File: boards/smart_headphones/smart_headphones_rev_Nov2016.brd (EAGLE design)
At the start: 51.7 x 39.4 mm, 14 parts, among them U1 ATMEGA328P_PDIP

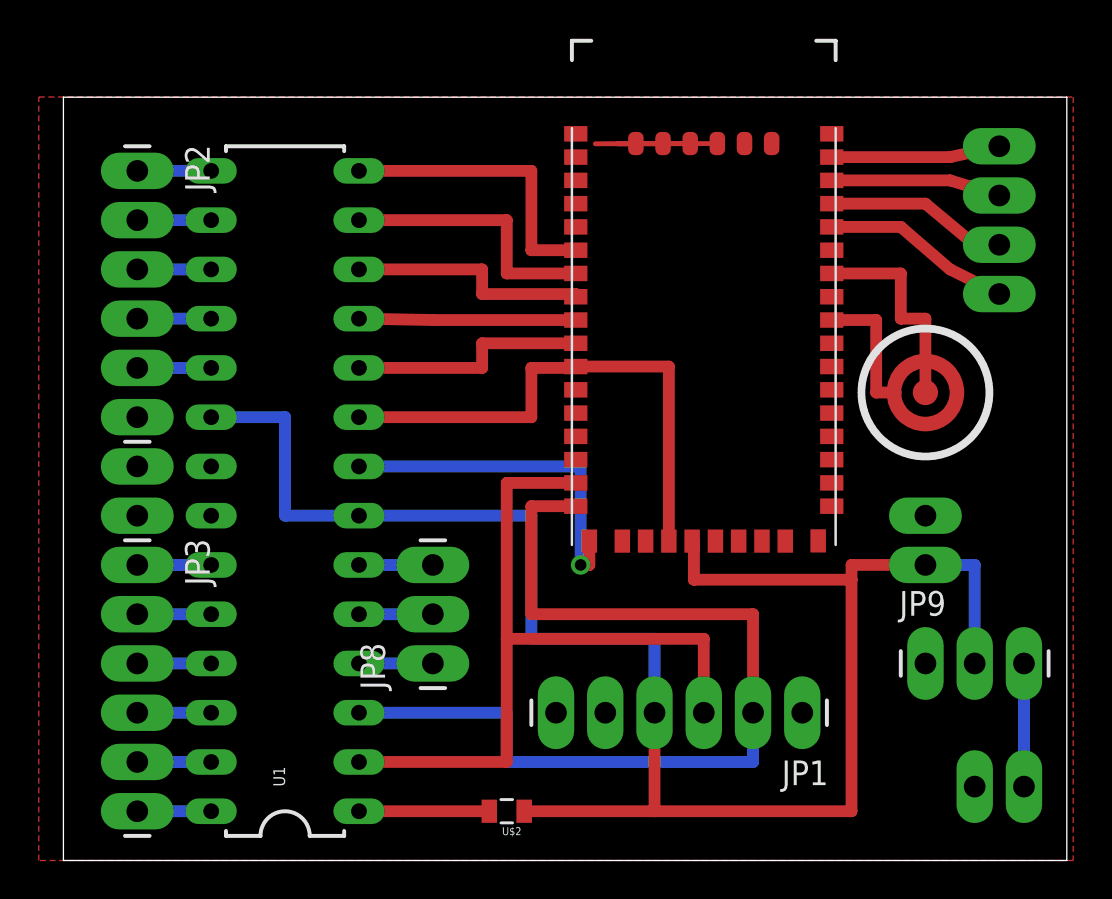
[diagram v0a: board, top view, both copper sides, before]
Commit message: Fixed bug (two control signals connected)
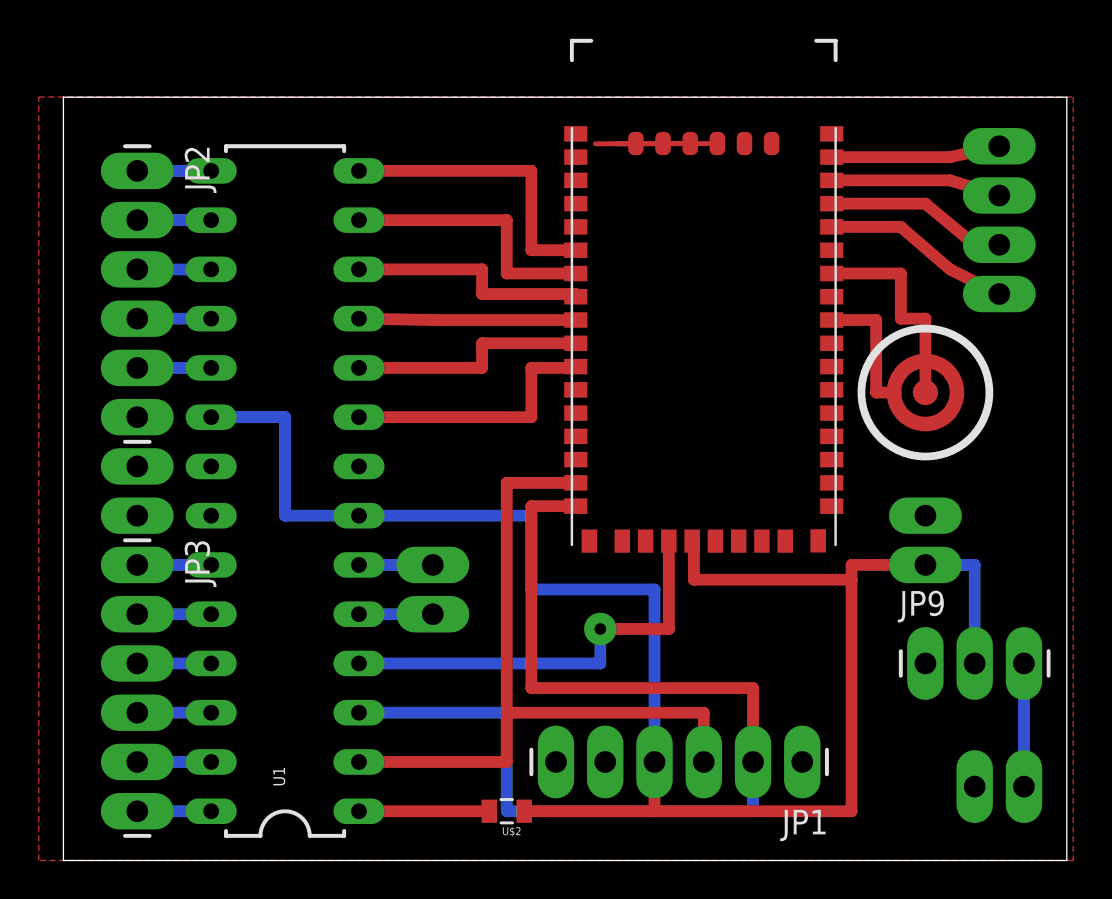
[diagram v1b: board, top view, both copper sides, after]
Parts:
- JP8: value (none) -> M02PTH3; device Finn-lbr-rev1:1X03_LONGPADS -> Finn-lbr-rev1:1X02_LONGPADS
- moved JP1 2.54 mm to (38.1, 24.1)
- moved JP8 2.54 mm to (19.1, 31.8)
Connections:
- removed net N$17: JP8.1, U1.4
- new net PWREN: U$1.19, U1.4
- net N$18: now also JP8.1; no longer JP8.2
- net N$19: now also JP8.2; no longer JP8.3
- net PB6: no longer U$1.19
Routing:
- net PWREN: track 0.00 -> 22.3 mm, vias 0 -> 1
- net GND: track 28.2 -> 10.0 mm, vias 1 -> 0
- net PB6: track 27.6 -> 13.8 mm
- net N$10: track 49.8 -> 54.9 mm
- net N$17: track 3.81 -> 0.00 mm
- net N$5: track 39.5 -> 38.3 mm
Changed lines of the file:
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@@
 <?xml version="1.0" encoding="utf-8"?>
 <!DOCTYPE eagle SYSTEM "eagle.dtd">
-<eagle version="7.1.0">
+<eagle version="7.7.0">
 <drawing>
 <settings>
@@
 </autorouter>
 <elements>
-<element name="JP1" library="Finn-lbr-rev1" package="1X06_LONGPADS" value="" x="38.1" y="26.67" rot="R180"/>
+<element name="JP1" library="Finn-lbr-rev1" package="1X06_LONGPADS" value="" x="38.1" y="24.13" rot="R180"/>
 <element name="JP3" library="Finn-lbr-rev1" package="1X06_LONGPADS" value="" x="3.81" y="34.29" rot="R270"/>
 <element name="U$1" library="Finn-lbr-rev1" package="RN-52" value="BLUETOOTH-RN-52" x="33.02" y="46.99"/>
@@
 <element name="JP6" library="Finn-lbr-rev1" package="1X02_LONGPADS" value="M02PTH3" x="44.45" y="36.83" rot="R270"/>
 <element name="JP7" library="Finn-lbr-rev1" package="1X02_LONGPADS" value="M02PTH3" x="3.81" y="39.37" rot="R270"/>
-<element name="JP8" library="Finn-lbr-rev1" package="1X03_LONGPADS" value="" x="19.05" y="29.21" rot="R90"/>
 <element name="JP9" library="Finn-lbr-rev1" package="1X03_LONGPADS" value="" x="44.45" y="29.21"/>
 <element name="JP10" library="Finn-lbr-rev1" package="1X02_LONGPADS" value="M02PTH3" x="49.53" y="22.86" rot="R180"/>
+<element name="JP8" library="Finn-lbr-rev1" package="1X02_LONGPADS" value="M02PTH3" x="19.05" y="31.75" rot="R90"/>
 </elements>
 <signals>
@@
 <contactref element="JP1" pad="4"/>
 <wire x1="23.76" y1="21.59" x2="30.48" y2="21.59" width="0.6096" layer="1"/>
-<wire x1="30.48" y1="21.59" x2="30.48" y2="26.67" width="0.6096" layer="1"/>
+<wire x1="30.48" y1="21.59" x2="30.48" y2="24.13" width="0.6096" layer="1"/>
 <wire x1="32.42" y1="35.52" x2="32.512" y2="35.52" width="0.6096" layer="1"/>
 <wire x1="32.512" y1="35.52" x2="32.512" y2="33.528" width="0.6096" layer="1"/>
@@
 <wire x1="40.64" y1="21.59" x2="30.48" y2="21.59" width="0.6096" layer="1"/>
 <wire x1="15.24" y1="36.83" x2="24.13" y2="36.83" width="0.6096" layer="16"/>
-<wire x1="24.13" y1="36.83" x2="24.13" y2="30.48" width="0.6096" layer="16"/>
-<wire x1="24.13" y1="30.48" x2="30.48" y2="30.48" width="0.6096" layer="16"/>
-<wire x1="30.48" y1="30.48" x2="30.48" y2="26.67" width="0.6096" layer="16"/>
+<wire x1="24.13" y1="36.83" x2="24.13" y2="33.02" width="0.6096" layer="16"/>
+<wire x1="24.13" y1="33.02" x2="30.48" y2="33.02" width="0.6096" layer="16"/>
+<wire x1="30.48" y1="33.02" x2="30.48" y2="24.13" width="0.6096" layer="16"/>
 <contactref element="U1" pad="20"/>
 <wire x1="7.62" y1="41.91" x2="11.43" y2="41.91" width="0.6096" layer="16"/>
@@
 </signal>
 <signal name="PB6">
-<contactref element="U$1" pad="19"/>
 <contactref element="U1" pad="9"/>
 <contactref element="U$1" pad="10"/>
@@
 <wire x1="24.13" y1="44.45" x2="26.42" y2="44.45" width="0.6096" layer="1"/>
 <wire x1="26.42" y1="44.45" x2="26.42" y2="44.52" width="0.6096" layer="1"/>
-<wire x1="26.42" y1="44.52" x2="31.22" y2="44.52" width="0.6096" layer="1"/>
-<wire x1="31.22" y1="44.52" x2="31.22" y2="35.52" width="0.6096" layer="1"/>
 </signal>
 <signal name="PB0">
@@
 <wire x1="28.575" y1="56.007" x2="33.72" y2="56.02" width="0.254" layer="1"/>
 <contactref element="JP2" pad="6"/>
-<wire x1="15.24" y1="39.37" x2="26.67" y2="39.37" width="0.6096" layer="16"/>
-<wire x1="26.67" y1="39.37" x2="26.67" y2="34.29" width="0.6096" layer="16"/>
-<via x="26.67" y="34.29" extent="1-16" drill="0.6" shape="square"/>
-<wire x1="26.67" y1="34.29" x2="27.12" y2="34.29" width="0.6096" layer="1"/>
-<wire x1="27.12" y1="34.29" x2="27.12" y2="35.52" width="0.6096" layer="1"/>
 <contactref element="JP7" pad="1"/>
 <contactref element="JP7" pad="2"/>
@@
 <contactref element="JP1" pad="3"/>
 <wire x1="26.42" y1="38.52" x2="22.86" y2="38.52" width="0.6096" layer="1"/>
-<wire x1="22.86" y1="38.52" x2="22.86" y2="30.48" width="0.6096" layer="1"/>
-<wire x1="22.86" y1="30.48" x2="33.02" y2="30.48" width="0.6096" layer="1"/>
-<wire x1="33.02" y1="30.48" x2="33.02" y2="26.67" width="0.6096" layer="1"/>
+<wire x1="22.86" y1="38.52" x2="22.86" y2="26.67" width="0.6096" layer="1"/>
+<wire x1="22.86" y1="26.67" x2="33.02" y2="26.67" width="0.6096" layer="1"/>
+<wire x1="33.02" y1="26.67" x2="33.02" y2="24.13" width="0.6096" layer="1"/>
 <wire x1="15.24" y1="24.13" x2="22.86" y2="24.13" width="0.6096" layer="1"/>
-<wire x1="22.86" y1="24.13" x2="22.86" y2="30.48" width="0.6096" layer="1"/>
+<wire x1="22.86" y1="24.13" x2="22.86" y2="26.67" width="0.6096" layer="1"/>
 </signal>
 <signal name="N$10">
@@
 <contactref element="JP1" pad="2"/>
 <wire x1="26.42" y1="37.32" x2="24.13" y2="37.32" width="0.6096" layer="1"/>
-<wire x1="24.13" y1="37.32" x2="24.13" y2="31.75" width="0.6096" layer="1"/>
-<wire x1="24.13" y1="31.75" x2="35.56" y2="31.75" width="0.6096" layer="1"/>
-<wire x1="35.56" y1="31.75" x2="35.56" y2="26.67" width="0.6096" layer="1"/>
+<wire x1="24.13" y1="37.32" x2="24.13" y2="27.94" width="0.6096" layer="1"/>
+<wire x1="24.13" y1="27.94" x2="35.56" y2="27.94" width="0.6096" layer="1"/>
+<wire x1="35.56" y1="27.94" x2="35.56" y2="24.13" width="0.6096" layer="1"/>
 <wire x1="15.24" y1="26.67" x2="22.86" y2="26.67" width="0.6096" layer="16"/>
-<wire x1="22.86" y1="26.67" x2="22.86" y2="24.13" width="0.6096" layer="16"/>
-<wire x1="22.86" y1="24.13" x2="35.56" y2="24.13" width="0.6096" layer="16"/>
-<wire x1="35.56" y1="24.13" x2="35.56" y2="26.67" width="0.6096" layer="16"/>
+<wire x1="22.86" y1="26.67" x2="22.86" y2="21.59" width="0.6096" layer="16"/>
+<wire x1="22.86" y1="21.59" x2="35.56" y2="21.59" width="0.6096" layer="16"/>
+<wire x1="35.56" y1="21.59" x2="35.56" y2="24.13" width="0.6096" layer="16"/>
 </signal>
 <signal name="N$1">
@@
 <wire x1="45.72" y1="54.12" x2="48.26" y2="53.34" width="0.6096" layer="1"/>
 </signal>
-<signal name="N$17">
-<contactref element="U1" pad="4"/>
-<contactref element="JP8" pad="1"/>
-<wire x1="15.24" y1="29.21" x2="19.05" y2="29.21" width="0.6096" layer="16"/>
-</signal>
 <signal name="N$18">
 <contactref element="U1" pad="5"/>
-<contactref element="JP8" pad="2"/>
+<contactref element="JP8" pad="1"/>
 <wire x1="15.24" y1="31.75" x2="19.05" y2="31.75" width="0.6096" layer="16"/>
 </signal>
 <signal name="N$19">
 <contactref element="U1" pad="6"/>
-<contactref element="JP8" pad="3"/>
+<contactref element="JP8" pad="2"/>
 <wire x1="15.24" y1="34.29" x2="19.05" y2="34.29" width="0.6096" layer="16"/>
 </signal>
@@
 <wire x1="49.53" y1="22.86" x2="49.53" y2="29.21" width="0.6096" layer="16"/>
 </signal>
+<signal name="PWREN">
+<contactref element="U$1" pad="19"/>
+<contactref element="U1" pad="4"/>
+<wire x1="15.24" y1="29.21" x2="27.686" y2="29.21" width="0.6096" layer="16"/>
+<wire x1="27.686" y1="29.21" x2="27.686" y2="30.988" width="0.6096" layer="16"/>
+<via x="27.686" y="30.988" extent="1-16" drill="0.6" diameter="1.6764" shape="octagon"/>
+<wire x1="27.686" y1="30.988" x2="31.22" y2="30.988" width="0.6096" layer="1"/>
+<wire x1="31.22" y1="30.988" x2="31.22" y2="35.52" width="0.6096" layer="1"/>
+</signal>
 </signals>
